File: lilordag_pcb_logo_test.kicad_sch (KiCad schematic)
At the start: 59 parts, among them Q1 BC846, Q2 BC846, SW1 PCM12SMTR

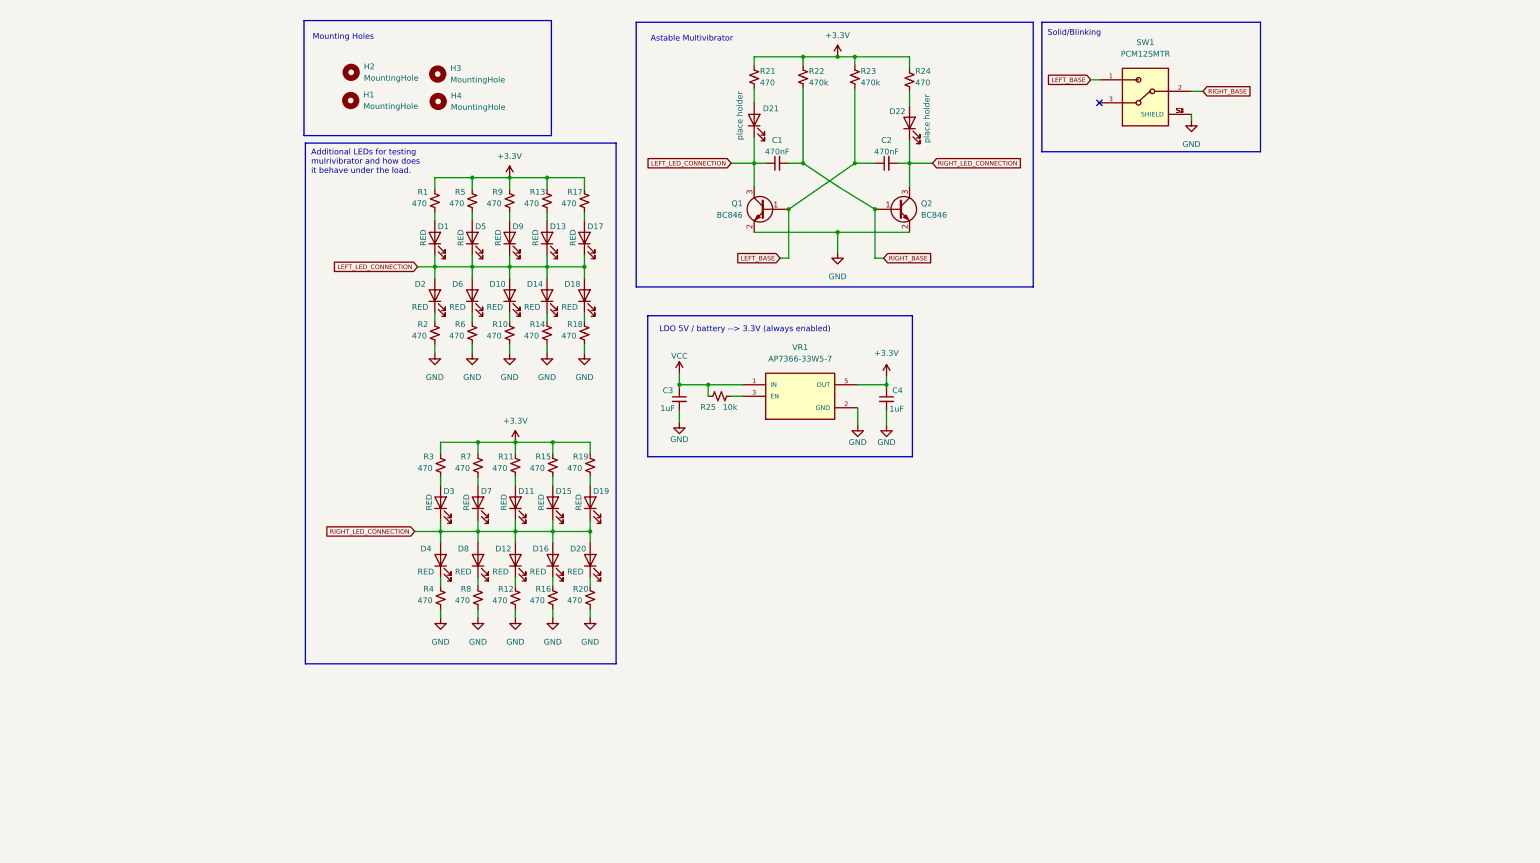
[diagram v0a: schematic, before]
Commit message: Added npn LED drivers.
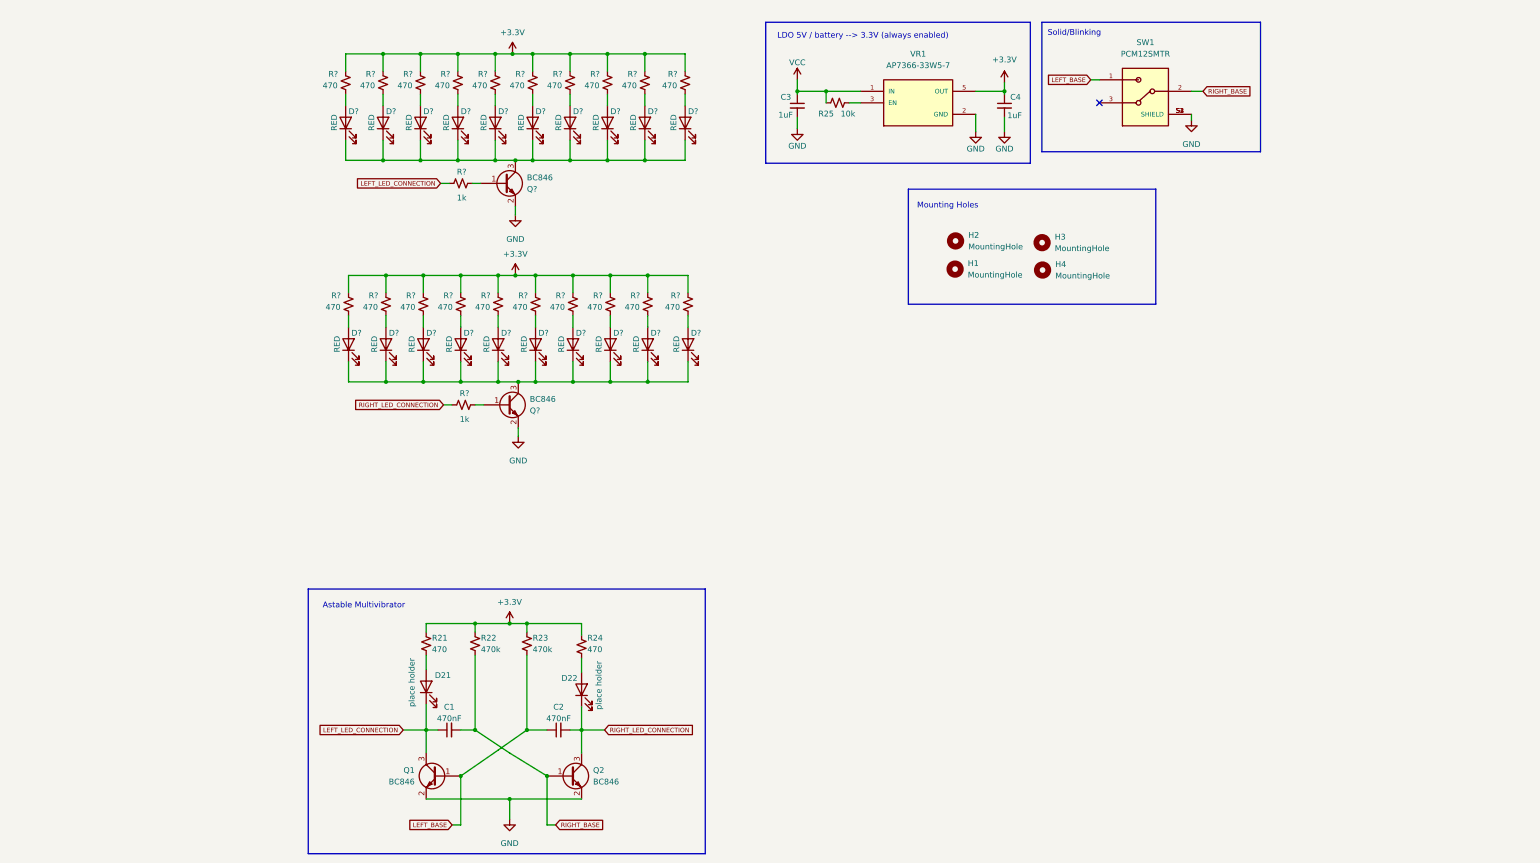
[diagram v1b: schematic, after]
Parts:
- removed D1, D10, D11, D12, D13, D14, D15, D16, D17, D18, D19, D2, D20, D3, D4, D5, D6, D7, D8, D9: RED, LED_SMD:LED_0603_1608Metric_Pad1.05x0.95mm_HandSolder, symbol Device:LED
- removed R1, R10, R11, R12, R13, R14, R15, R16, R17, R18, R19, R2, R20, R3, R4, R5, R6, R7, R8, R9: 470, Resistor_SMD:R_0603_1608Metric_Pad0.98x0.95mm_HandSolder, symbol Device:R_Small_US
- added D? (x20): RED, LED_SMD:LED_0603_1608Metric_Pad1.05x0.95mm_HandSolder, symbol Device:LED
- added Q? (x2): BC846, Package_TO_SOT_SMD:SOT-23, symbol Transistor_BJT:BC846
- added R? (x20): 470, Resistor_SMD:R_0603_1608Metric_Pad0.98x0.95mm_HandSolder, symbol Device:R_Small_US
- added R? (x2): 1k, Resistor_SMD:R_0603_1608Metric_Pad0.98x0.95mm_HandSolder, symbol Device:R_Small_US
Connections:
- net +3.3V: now also R?.1, R?.1, R?.1, R?.1, R?.1, R?.1, R?.1, R?.1, R?.1, R?.1, R?.1, R?.1, R?.1, R?.1, R?.1, R?.1, R?.1, R?.1, R?.1, R?.1
- net GND: now also Q?.2 (E), Q?.2 (E)
- net LEFT_LED_CONNECTION: now also R?.1
- net RIGHT_LED_CONNECTION: now also R?.1
- new net: D?.2 (A), R?.2 (x20)
- new net: D?.1 (K), D?.1 (K), D?.1 (K), D?.1 (K), D?.1 (K), D?.1 (K), D?.1 (K), D?.1 (K), D?.1 (K), D?.1 (K), Q?.3 (C) (x2)
- new net: Q?.1 (B), R?.2 (x2)
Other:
- note removed: "Additional LEDs for testing mulrivibrator and how does it behave under the load."
- moved on the sheet: C1, C2, C3, C4, D21, D22, H1, H2, H3, H4, Q1, Q2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

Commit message: Added PNP driver.
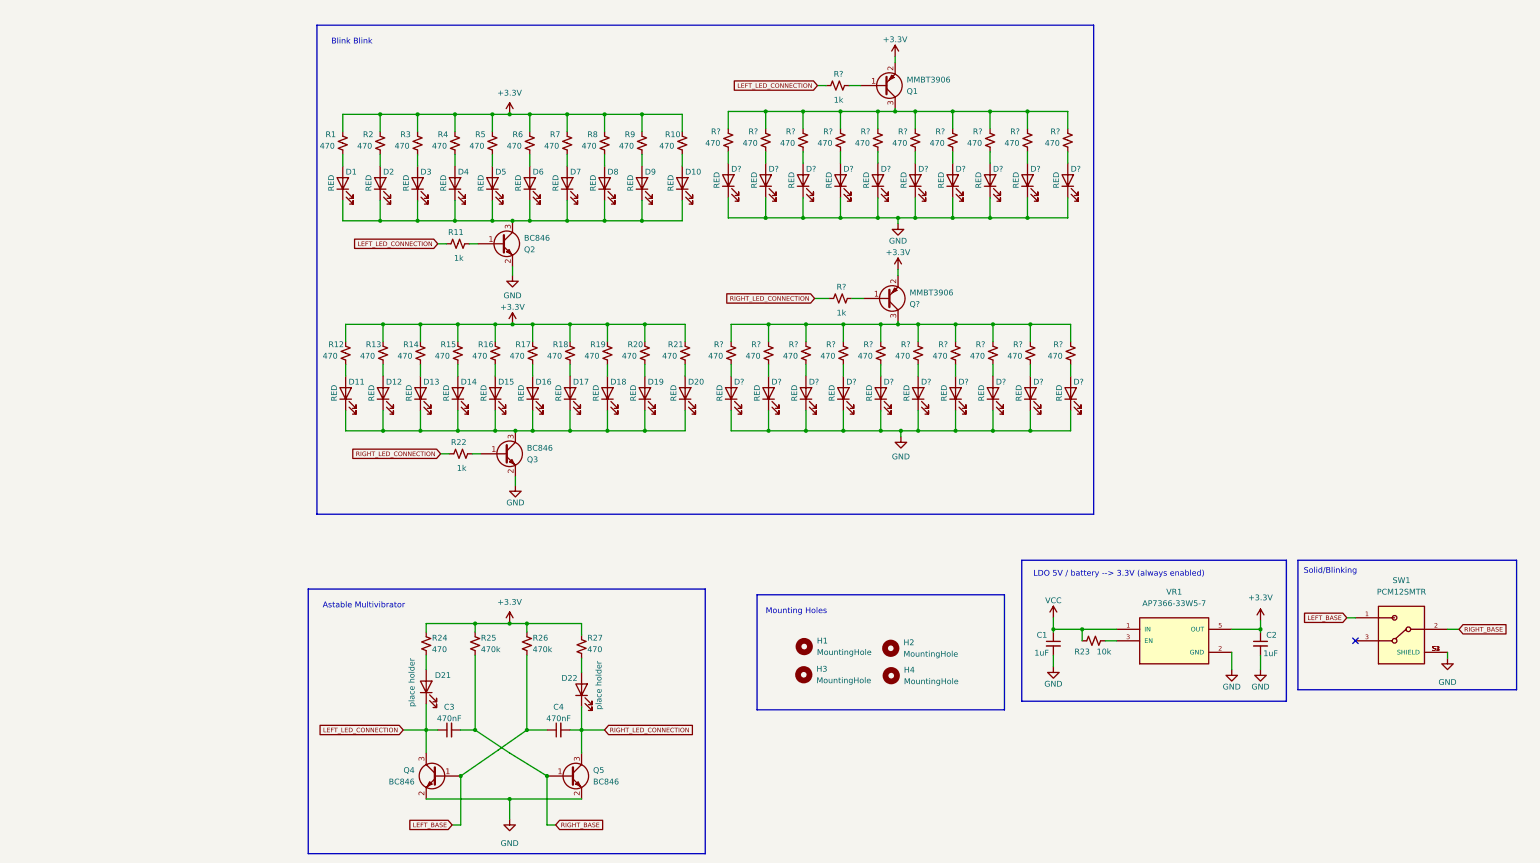
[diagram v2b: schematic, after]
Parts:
- added D? (x20): RED, LED_SMD:LED_0603_1608Metric_Pad1.05x0.95mm_HandSolder, symbol Device:LED
- added Q1, Q?: MMBT3906, Package_TO_SOT_SMD:SOT-23, symbol Transistor_BJT:MMBT3906
- added R? (x20): 470, Resistor_SMD:R_0603_1608Metric_Pad0.98x0.95mm_HandSolder, symbol Device:R_Small_US
- added R? (x2): 1k, Resistor_SMD:R_0603_1608Metric_Pad0.98x0.95mm_HandSolder, symbol Device:R_Small_US
- gave numbers to parts that had none: 44
- renumbered C3 to C1, C4 to C2, C1 to C3, C2 to C4, H2 to H1, H3 to H2, H1 to H3, Q1 to Q4, Q2 to Q5, R25 to R23, R21 to R24, R22 to R25, R23 to R26, R24 to R27
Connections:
- net +3.3V: now also Q1.2 (E), Q?.2 (E)
- net GND: now also D?.1 (K), D?.1 (K), D?.1 (K), D?.1 (K), D?.1 (K), D?.1 (K), D?.1 (K), D?.1 (K), D?.1 (K), D?.1 (K), D?.1 (K), D?.1 (K), D?.1 (K), D?.1 (K), D?.1 (K), D?.1 (K), D?.1 (K), D?.1 (K), D?.1 (K), D?.1 (K)
- net LEFT_LED_CONNECTION: now also R?.1
- net RIGHT_LED_CONNECTION: now also R?.1
- new net: Q1.3 (C), R?.1, R?.1, R?.1, R?.1, R?.1, R?.1, R?.1, R?.1, R?.1, R?.1
- new net: D?.2 (A), R?.2 (x20)
- new net: Q?.1 (B), R?.2
- new net: Q?.3 (C), R?.1, R?.1, R?.1, R?.1, R?.1, R?.1, R?.1, R?.1, R?.1, R?.1
- new net: Q1.1 (B), R?.2
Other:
- note added: "Blink Blink"
- moved on the sheet: C1, C2, D1, D10, D11, D12, D13, D14, D15, D16, D17, D18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

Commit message: Added USBC
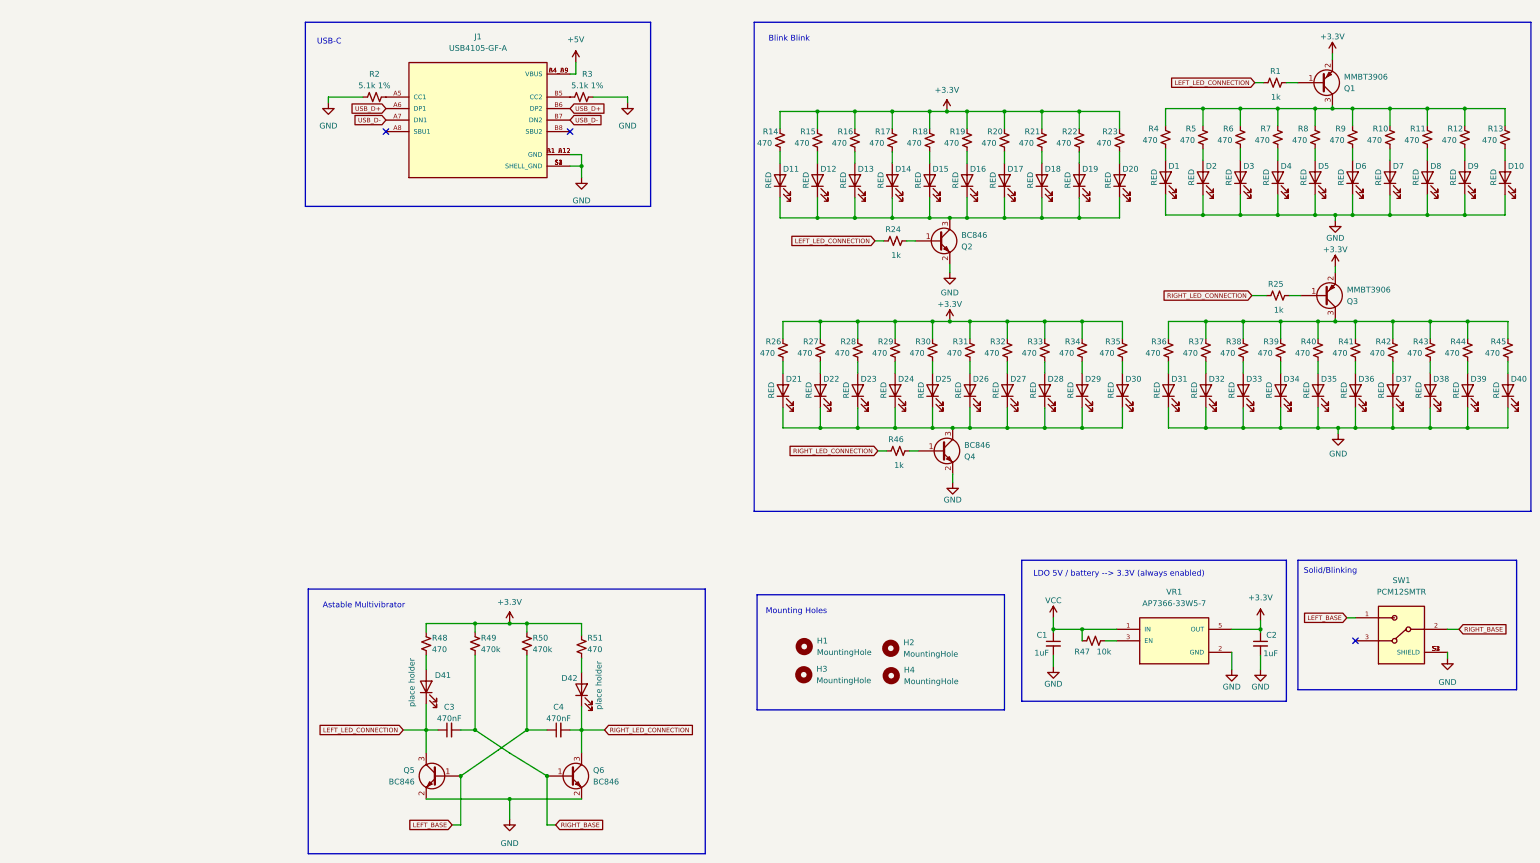
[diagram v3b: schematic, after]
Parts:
- added J1: USB4105-GF-A, USBC-USB4105-GF-A:GCT_USB4105-GF-A, symbol USB4105-GF-A:USB4105-GF-A
- added R2, R3: 5.1k 1%, Resistor_SMD:R_0603_1608Metric_Pad0.98x0.95mm_HandSolder, symbol Device:R_Small_US
- gave numbers to parts that had none: 43
- renumbered D1 to D11, D2 to D12, D3 to D13, D4 to D14, D5 to D15, D6 to D16, D7 to D17, D8 to D18, D9 to D19, D10 to D20, D11 to D21, D12 to D22, D13 to D23, D14 to D24, D15 to D25, D16 to D26, D17 to D27, D18 to D28, D19 to D29, D20 to D30, D21 to D41, D22 to D42, Q3 to Q4, Q4 to Q5, Q5 to Q6, R1 to R14, R2 to R15, R3 to R16, R4 to R17, R5 to R18, R6 to R19, R7 to R20, R8 to R21, R9 to R22, R10 to R23, R11 to R24, R12 to R26, R13 to R27, R14 to R28, R15 to R29, R16 to R30, R17 to R31, R18 to R32, R19 to R33, R20 to R34, R21 to R35, R22 to R46, R23 to R47, R24 to R48, R25 to R49, R26 to R50, R27 to R51
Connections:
- net GND: now also J1.A1_B12 (GND), J1.B1_A12 (GND), J1.S1 (SHELL_GND), J1.S2 (SHELL_GND), J1.S3 (SHELL_GND), J1.S4 (SHELL_GND), R2.1, R3.2
- new net: J1.A5 (CC1), R2.2
- new net: J1.B5 (CC2), R3.1
- new net +5V: J1.A4_B9 (VBUS), J1.B4_A9 (VBUS)
- new net USB_D+: J1.A6 (DP1), J1.B6 (DP2)
- new net USB_D-: J1.A7 (DN1), J1.B7 (DN2)
- no-connect marks 1 -> 3
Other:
- note added: "USB-C"
- moved on the sheet: D1, D10, D11, D12, D13, D14, D15, D16, D17, D18, D19, D2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

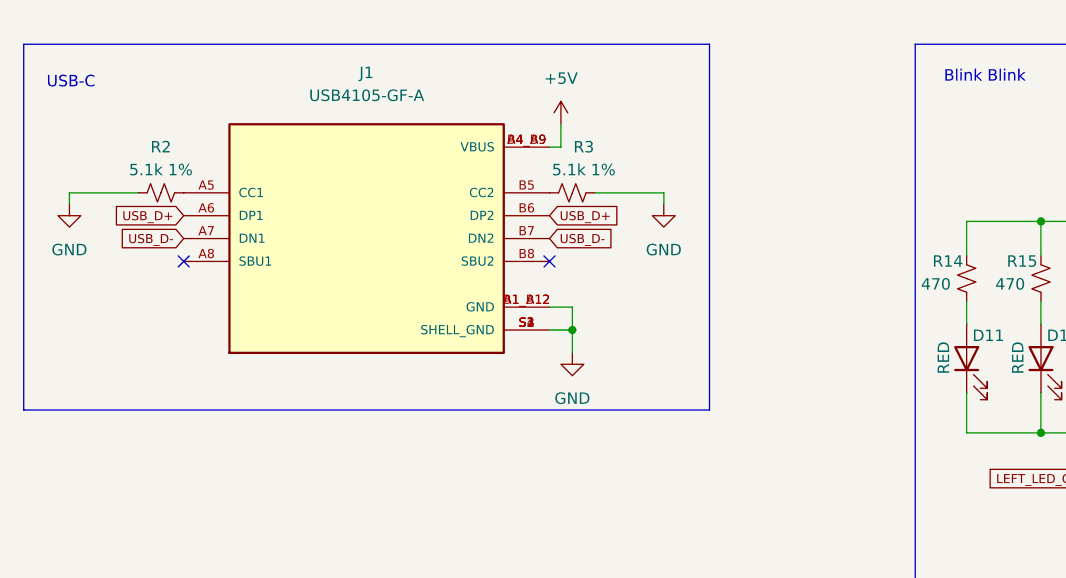
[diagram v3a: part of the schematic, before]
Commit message: Added 2 CR2032 battery holders.
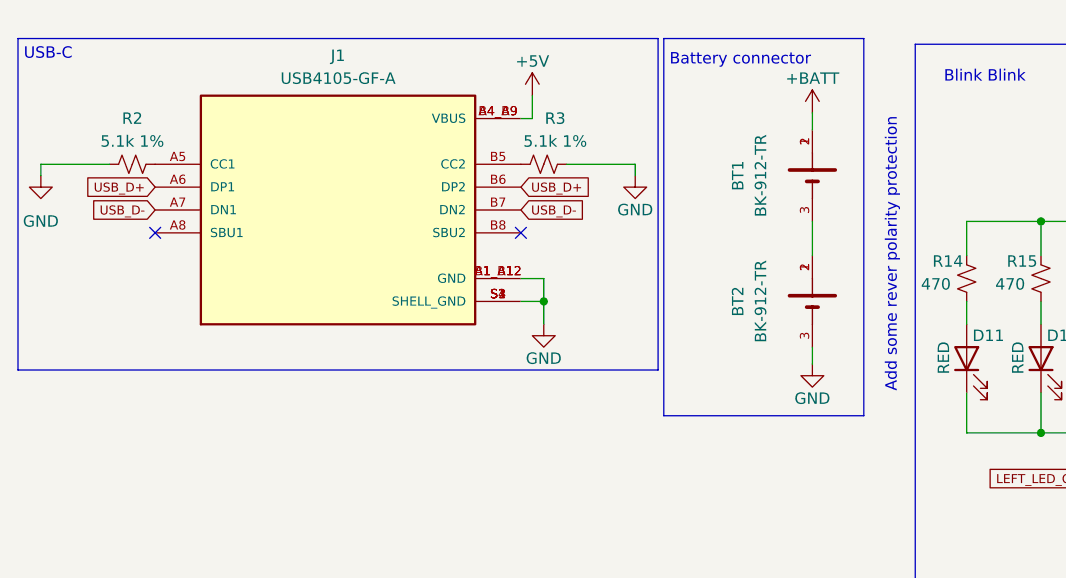
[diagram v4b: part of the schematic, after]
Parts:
- added BT1: BK-912-TR, BK-912-TR-batt-holder:MPD_BK-912-TR, symbol BK-912-TR:BK-912-TR
- added BT2: BK-912-TR, MPD_BK-912-TR, symbol BK-912-TR:BK-912-TR
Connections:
- net GND: now also BT2.3
- new net: BT1.3, BT2.1, BT2.2
- new net +BATT: BT1.1, BT1.2
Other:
- note added: "Add some rever polarity protection"
- note added: "Battery connector"
- moved on the sheet: J1, R2, R3

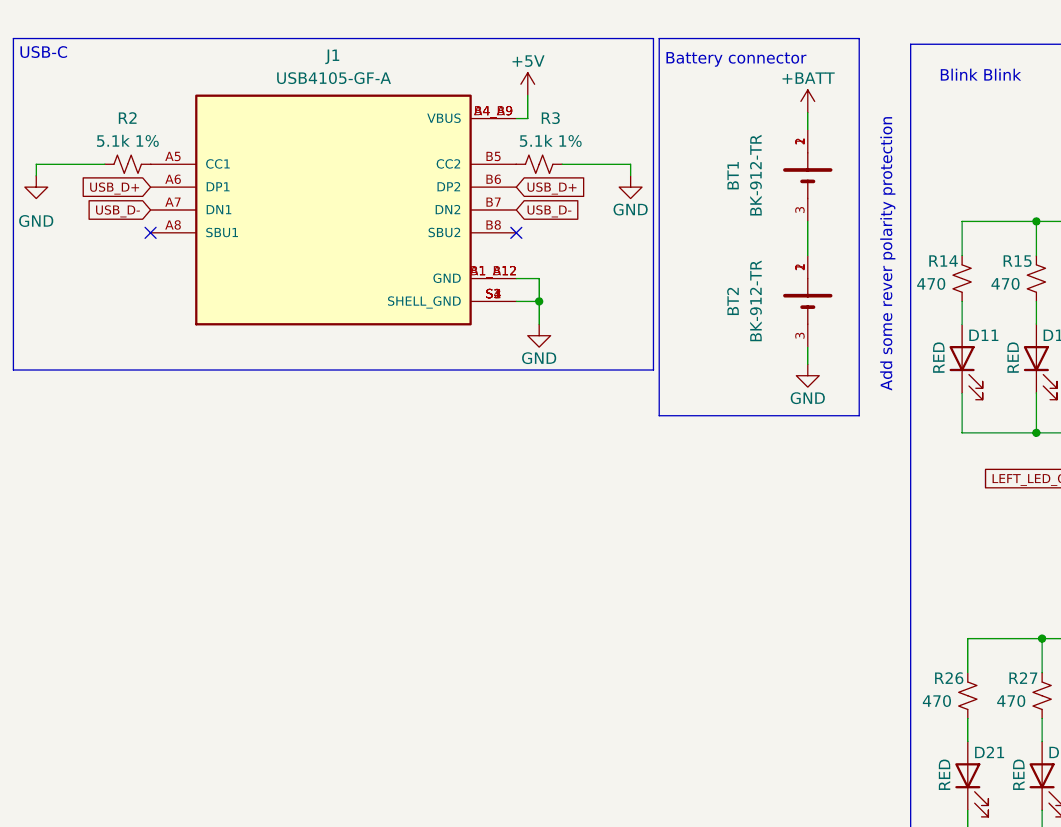
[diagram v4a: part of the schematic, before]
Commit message: Made a todo list on the schematic.
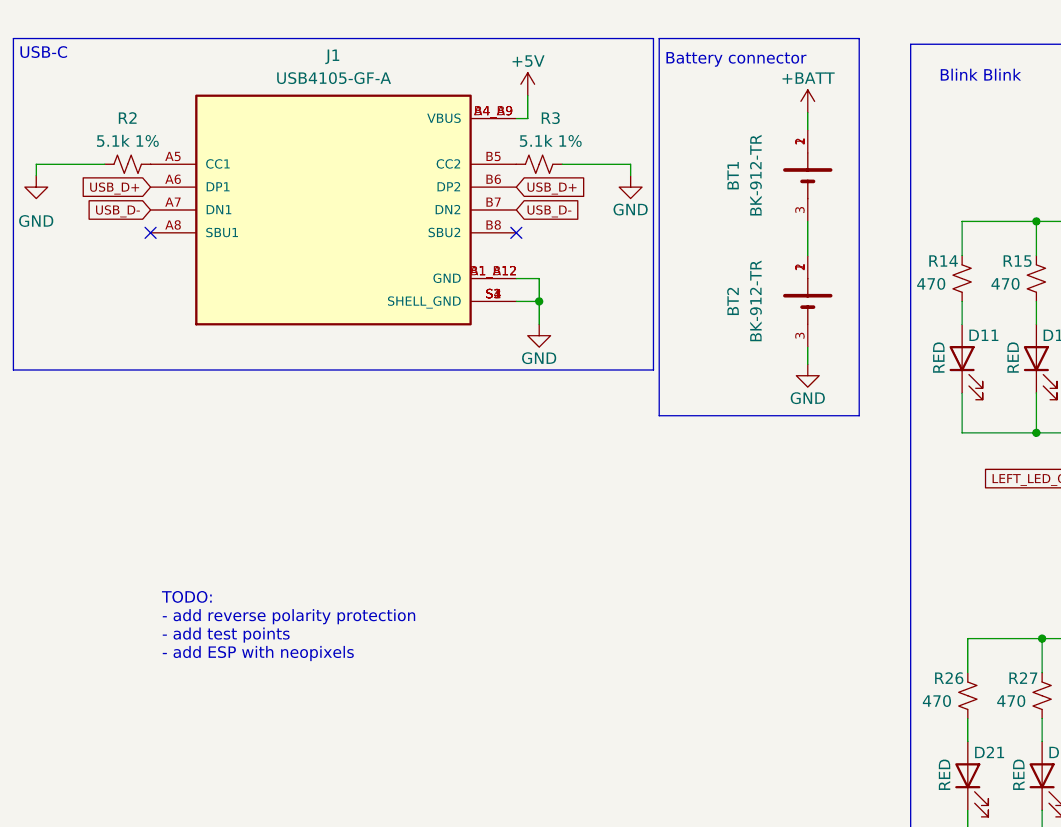
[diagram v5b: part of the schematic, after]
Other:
- note added: "TODO: - add reverse polarity protection - add test points - add ESP with neopixels"
- note removed: "Add some rever polarity protection"
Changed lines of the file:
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@@
     (effects (font (size 1.27 1.27)) (justify left bottom))
   )
-  (text "Add some rever polarity protection" (at 110.49 52.07 90)
+  (text "TODO:\n- add reverse polarity protection\n- add test points\n- add ESP with neopixels"
+    (at 29.21 81.915 0)
     (effects (font (size 1.27 1.27)) (justify left bottom))
   )
